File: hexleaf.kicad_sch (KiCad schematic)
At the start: 53 parts, among them IC1 ESP32-C3-FH4, J2 Conn_01x04, J5 Conn_01x08, J6 Conn_01x04, J7 Conn_01x08, SW1 SW_SPST, SW2 SW_SPST, Y1 ECS-400-10-37B2-CKM-TR

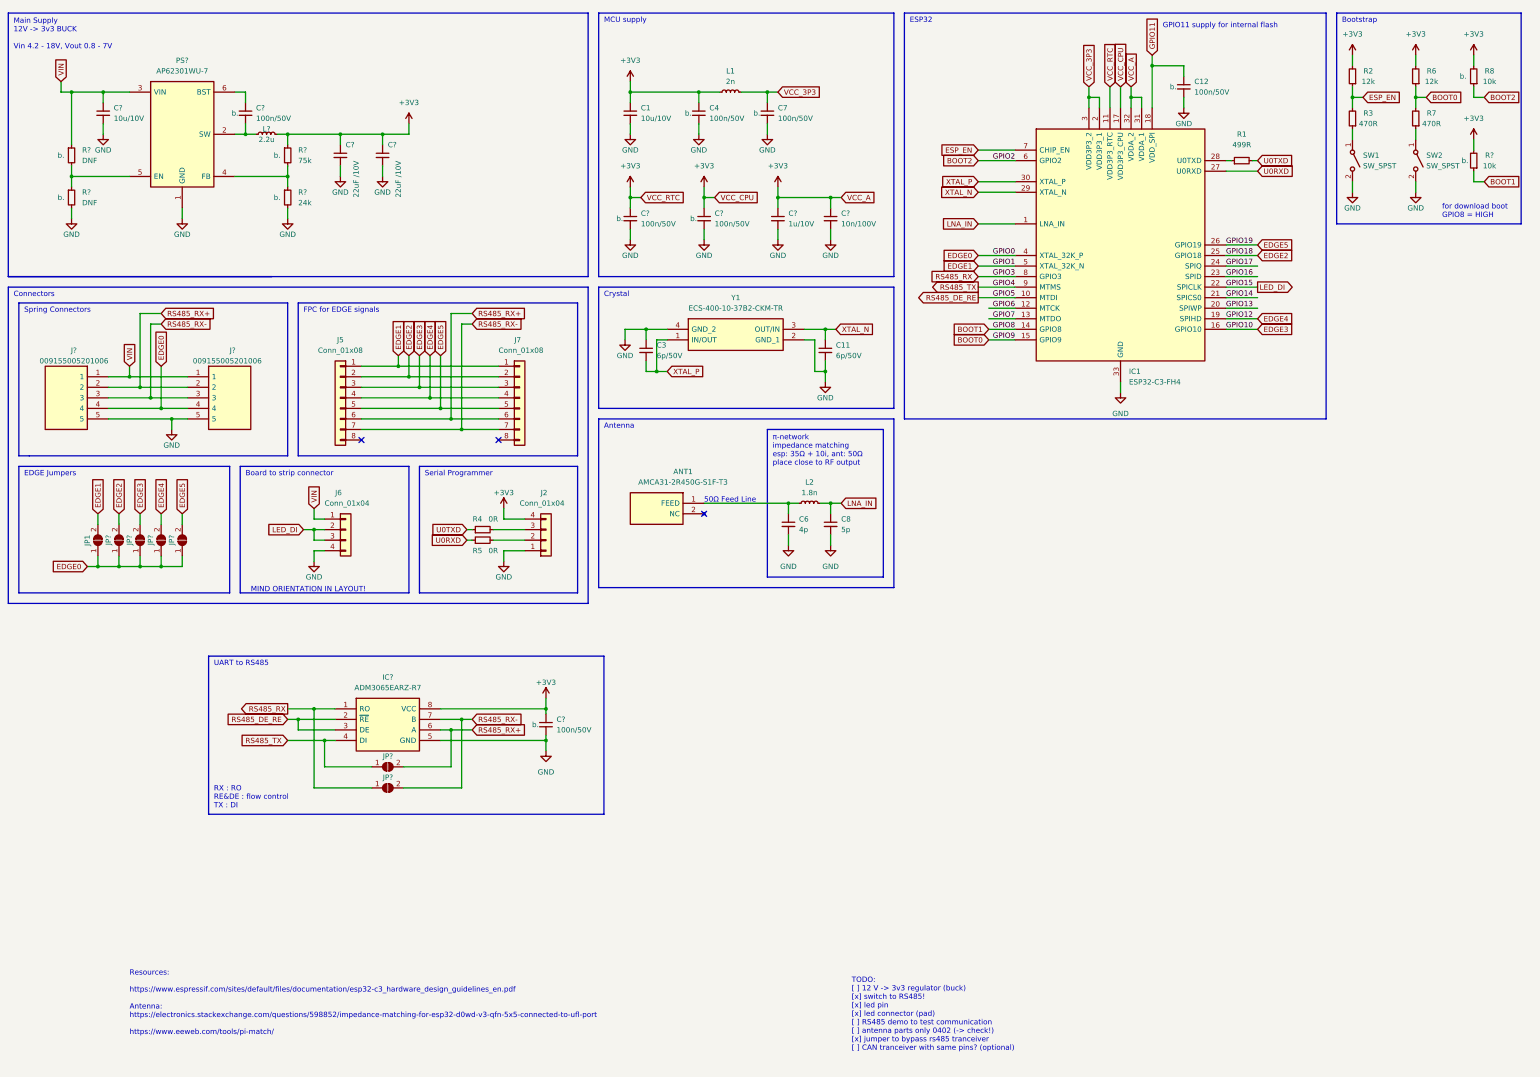
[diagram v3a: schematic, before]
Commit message: changed parts and ordered first batch for prototyping
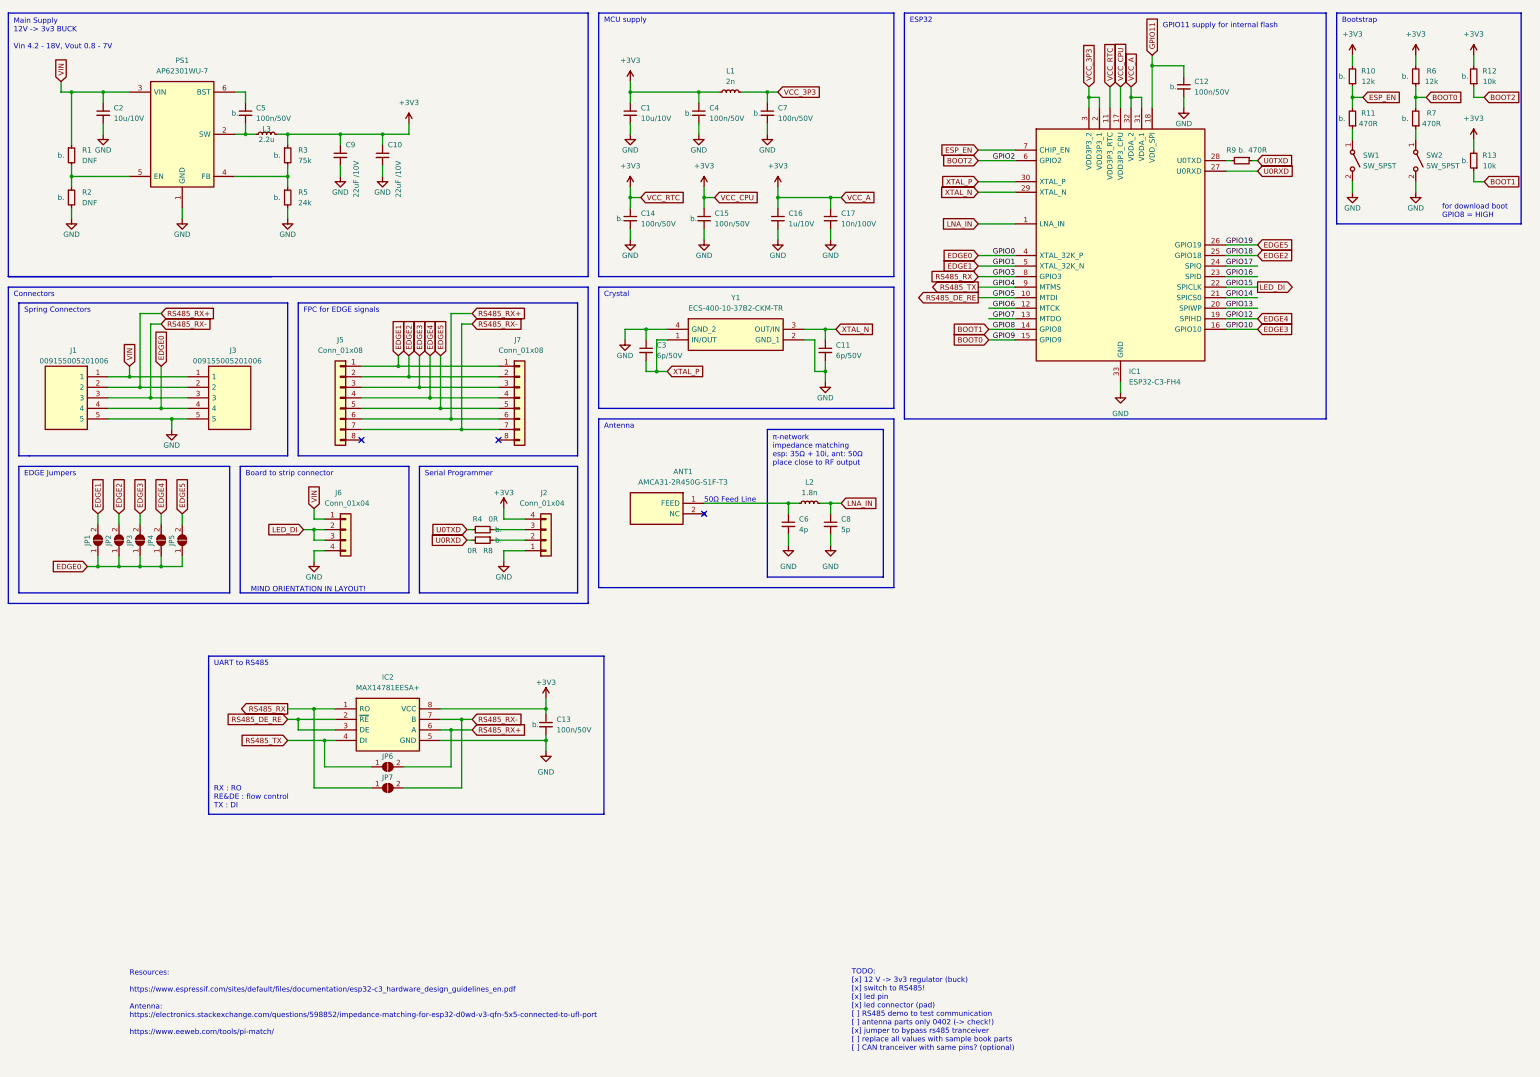
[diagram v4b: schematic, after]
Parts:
- removed IC?: ADM3065EARZ-R7, SOIC127P600X175-8N, symbol hexleaf:ADM3065EARZ-R7
- removed R1: 499R, Resistor_SMD:R_0603_1608Metric, symbol Device:R_Small
- removed R2: 12k, Resistor_SMD:R_0603_1608Metric, symbol Device:R_Small
- removed R3: 470R, Resistor_SMD:R_0603_1608Metric, symbol Device:R_Small
- removed R5: 0R, Resistor_SMD:R_0603_1608Metric, symbol Device:R_Small
- added IC2: MAX14781EESA+, hexleaf:SOIC127P600X175-8N, symbol hexleaf:MAX14781EESA+
- added R10: 12k, Resistor_SMD:R_0402_1005Metric, symbol Device:R_Small
- added R11, R9: 470R, Resistor_SMD:R_0402_1005Metric, symbol Device:R_Small
- added R12: 10k, Resistor_SMD:R_0805_2012Metric, symbol Device:R_Small
- C11, C3: footprint Capacitor_SMD:C_0603_1608Metric -> Capacitor_SMD:C_0402_1005Metric; MFN 791-0603N6R0D500CT -> 81-GRM1555C1H6R0WA1D
- C6: footprint Capacitor_SMD:C_0603_1608Metric -> Capacitor_SMD:C_0402_1005Metric; MFN 81-GQM1875C2E4R0WB2D -> 81-GRM1555C1H4R0WA1D
- C8: footprint Capacitor_SMD:C_0603_1608Metric -> Capacitor_SMD:C_0402_1005Metric; MFN 81-GRM1885C1H5R0WA1D -> 81-GRM1555C1H5R0WA1D
- L2: footprint Inductor_SMD:L_0603_1608Metric -> Inductor_SMD:L_0402_1005Metric; MFN 710-7447860018G -> 81-LQG15HS1N8B02D
- R13: renamed from R?; MFN 279-CRGCQ0805F10K -> 603-RC0402FR-0710KL
- R4: footprint Resistor_SMD:R_0603_1608Metric -> Resistor_SMD:R_0402_1005Metric; MFN 652-CR0603AJ/-000ELF -> 603-RC0402FR-070RL; in stock (none) -> b.
- R6: footprint Resistor_SMD:R_0603_1608Metric -> Resistor_SMD:R_0402_1005Metric; MFN 71-CRCW060312K0FKEAC -> 603-RC0402FR-0712KL; in stock (none) -> b.
- R7: footprint Resistor_SMD:R_0603_1608Metric -> Resistor_SMD:R_0402_1005Metric; MFN 660-RK73B1JTTDD471J -> 603-RC0402FR-07470RL; in stock (none) -> b.
- R8: value 10k -> 0R; footprint Resistor_SMD:R_0805_2012Metric -> Resistor_SMD:R_0402_1005Metric; MFN 279-CRGCQ0805F10K -> 603-RC0402FR-070RL
- gave numbers to parts that had none: 23
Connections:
- net +3V3: now also IC2.8 (VCC), R10.2, R12.2; no longer R8.2
- net BOOT2: now also R12.1; no longer R8.1
- net ESP_EN: now also R10.1, R11.2
- net GND: now also IC2.5 (GND)
- net RS485_DE_RE: now also IC2.2 (~{RE}), IC2.3 (DE)
- net RS485_RX: now also IC2.1 (RO)
- net RS485_RX+: now also IC2.6 (A)
- net RS485_RX-: now also IC2.7 (B)
- net RS485_TX: now also IC2.4 (DI)
- net U0RXD: now also R8.2
- net U0TXD: now also R9.1
- net at SW1.1 (A): now also R11.1
- net at J2.2 (Pin_2): now also R8.1
- net at IC1.28 (U0TXD): now also R9.2
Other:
- note added: "TODO: [x] 12 V -> 3v3 regulator (buck) [x] switch to RS485! [x] led pin [x] led connector (pad) [ ] RS485 demo to test communication [ ] antenna parts only 0402 (-> check!) [x] jumper to bypass rs485 tranceiver [ ] replace all values with sample book parts [ ] CAN tranceiver with same pins? (optional)"
- note removed: "TODO: [ ] 12 V -> 3v3 regulator (buck) [x] switch to RS485! [x] led pin [x] led connector (pad) [ ] RS485 demo to test communication [ ] antenna parts only 0402 (-> check!) [x] jumper to bypass rs485 tranceiver [ ] CAN tranceiver with same pins? (optional)"
